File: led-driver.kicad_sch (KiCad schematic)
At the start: 44 parts, among them U1 PAM2863, U2 PAM2863, U3 PAM2863, U4 PAM2863

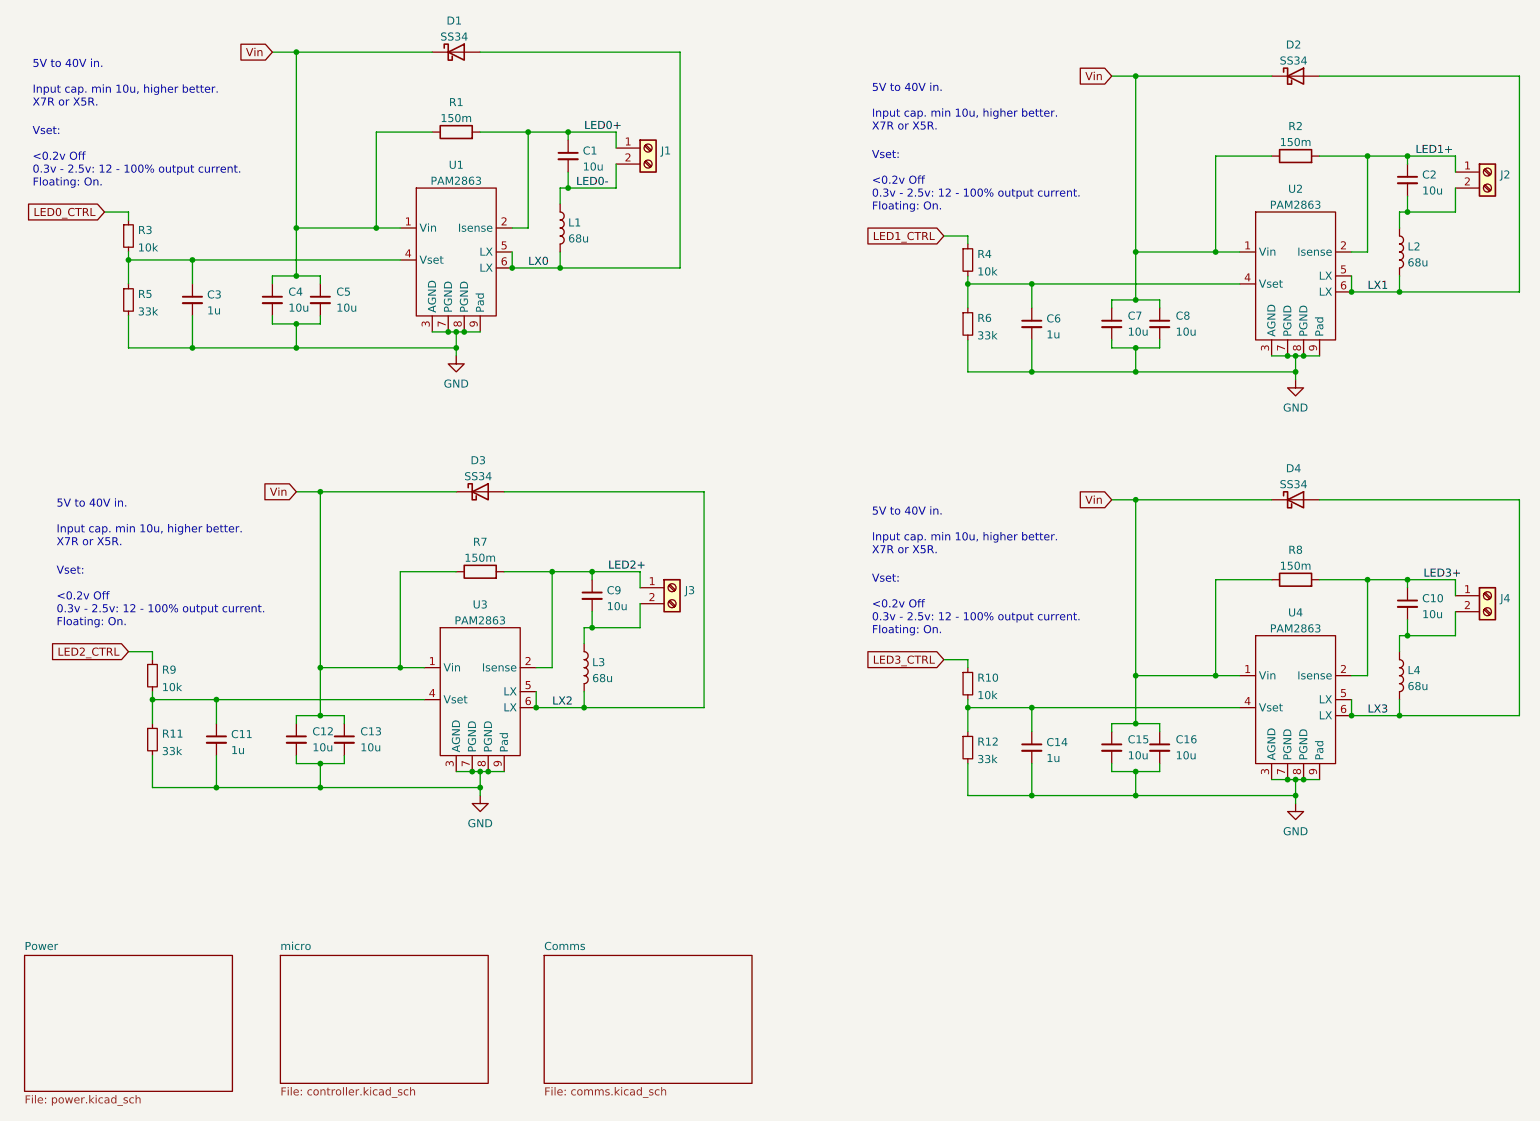
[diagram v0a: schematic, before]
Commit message: Schematic cleanup and readme improvement.
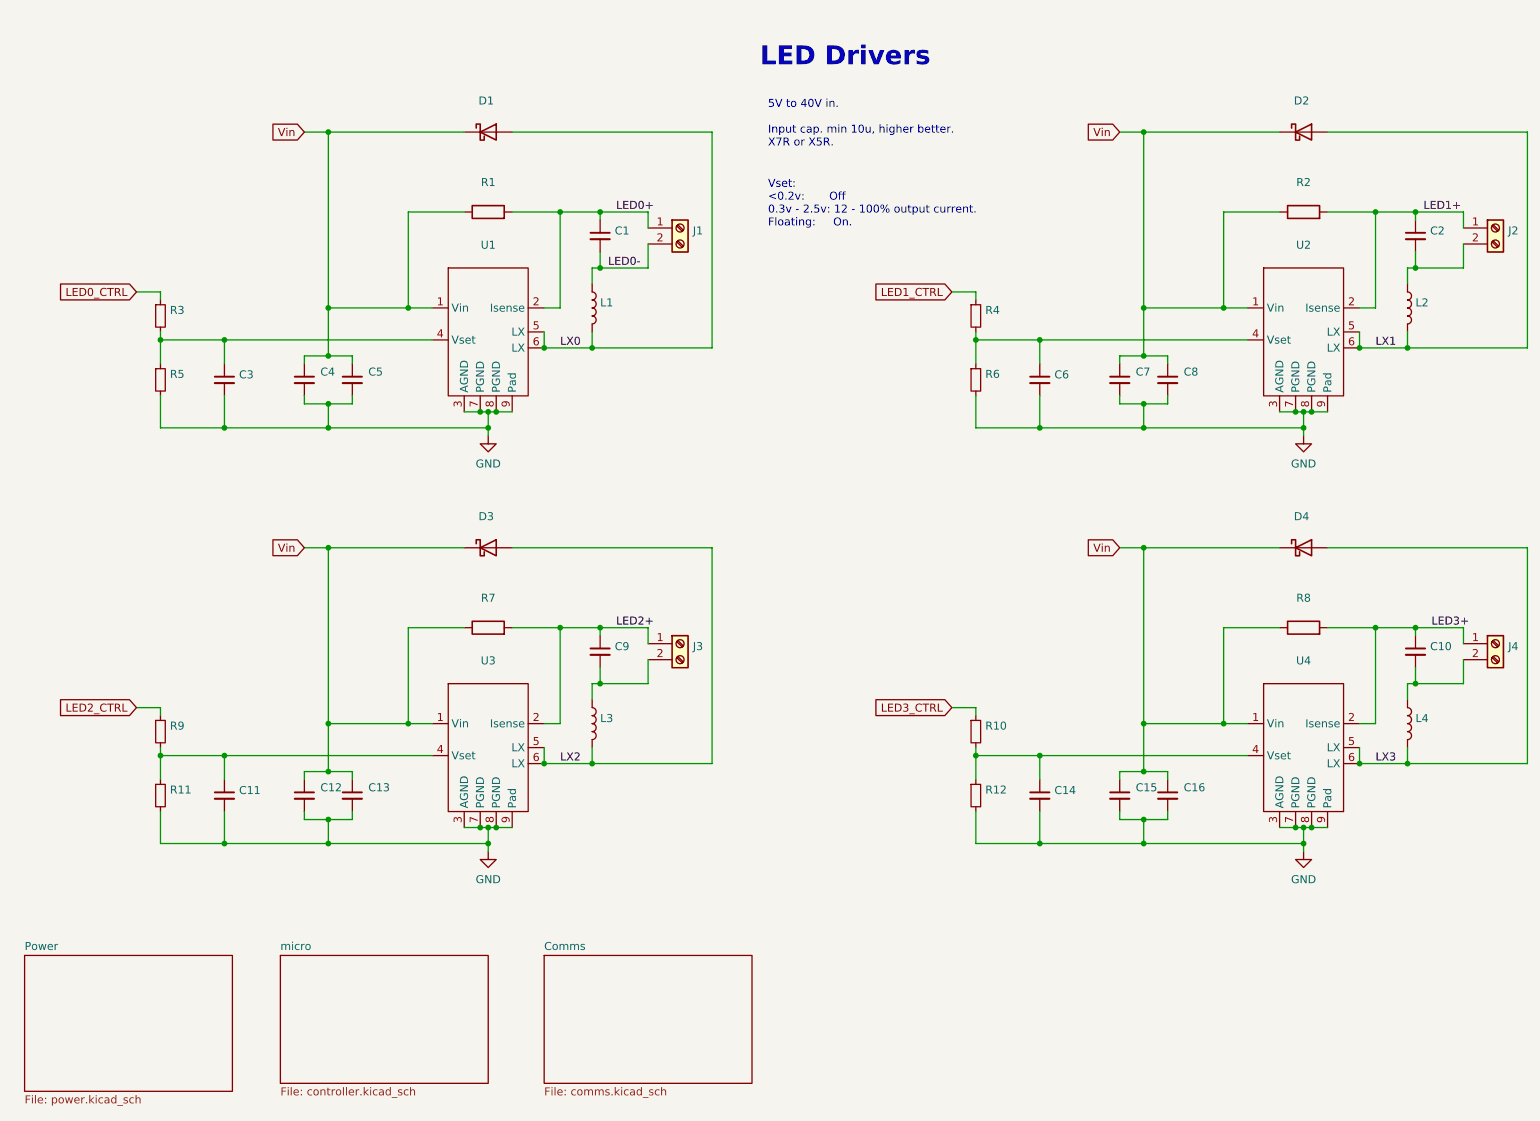
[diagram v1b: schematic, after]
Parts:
- C1, C10, C12, C13, C15, C16, C2, C4, C5, C7, C8, C9: value 10u -> (none); footprint Capacitor_SMD:C_1206_3216Metric_Pad1.33x1.80mm_HandSolder -> (none)
- C11, C14, C3, C6: value 1u -> (none); footprint Capacitor_SMD:C_0805_2012Metric -> (none)
- D1, D2, D3, D4: value SS34 -> (none); footprint Diode_SMD:D_SMA -> (none); Note Only needs 1A peak. -> Only needs 1A peak (for 700mA out anyway).
- J1, J2, J3, J4: value ~ -> (none); footprint river:TerminalBlock_KEFENG_Blue_2 -> (none)
- L1, L2, L3, L4: value 68u -> (none); footprint river:Inductor_SMD_10.2x11.0x5 -> (none)
- R1, R2, R7, R8: value 150m -> (none); footprint Resistor_SMD:R_2010_5025Metric_Pad1.40x2.65mm_HandSolder -> (none)
- R10, R3, R4, R9: value 10k -> (none); footprint Resistor_SMD:R_0805_2012Metric -> (none)
- R11, R12, R5, R6: value 33k -> (none); footprint Resistor_SMD:R_0805_2012Metric -> (none)
- U1, U2, U3, U4: value PAM2863 -> (none); footprint river:HSOP-8-1EP_3.9x4.9mm_P1.27mm_EP2.41x3.1mm_ThermalVias_0.3mm -> (none)
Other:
- note added: "LED Drivers"
- note added: "Vset: <0.2v: Off 0.3v - 2.5v: 12 - 100% output current. Floating: On."
- note removed: "Vset: <0.2v Off 0.3v - 2.5v: 12 - 100% output current. Floating: On."
- company: (none) -> River Cat
- title: (none) -> Plant Light LED Driver
- moved on the sheet: C1, C10, C11, C12, C13, C14, C15, C16, C2, C3, C4, C5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
